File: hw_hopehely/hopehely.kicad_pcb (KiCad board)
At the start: 2 copper layers, 48.3 x 55.8 mm, 39 parts, among them J1 Conn_2Rows-05Pins, Q1 AO3401A, Q2 AO3401A, Q3 AO3401A, SW1 SW_DPST_x2, T1 Tab, U1 PY32F002AF15P6TU

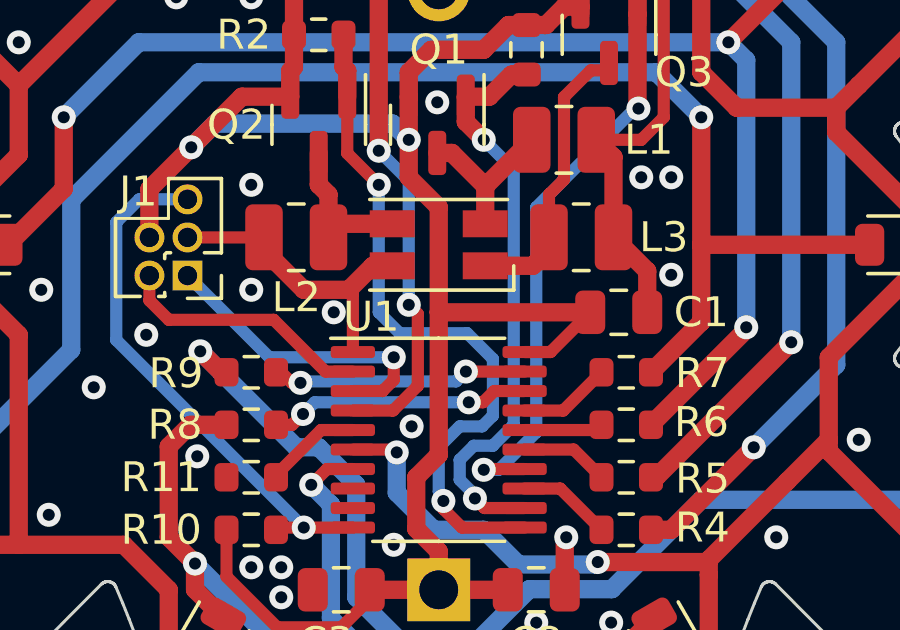
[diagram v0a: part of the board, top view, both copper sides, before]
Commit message: Footprint fix for JLCPCB assembly.
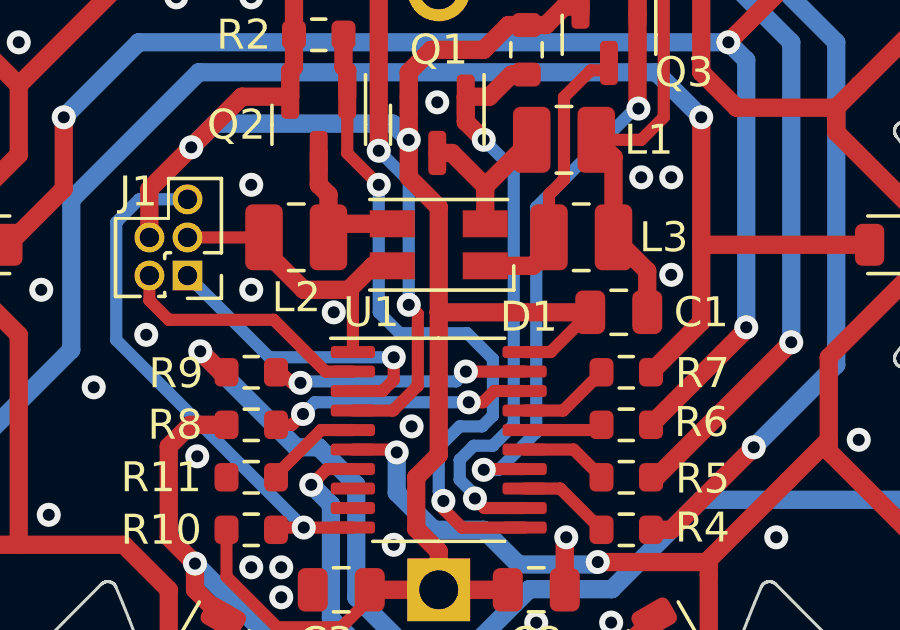
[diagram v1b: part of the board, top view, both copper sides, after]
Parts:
- D1: footprint LED_SMD:LED_RGB_Wuerth-PLCC4_3.2x2.8mm_150141M173100 -> karifa:LED_RGB_Wuerth-PLCC4_3.2x2.8mm_150141M173100
- U1: footprint Package_SO:TSSOP-20_4.4x6.5mm_P0.65mm -> karifa:TSSOP-20_4.4x6.5mm_P0.65mm
- turned D1 to 0 degrees
- turned U1 to 180 degrees

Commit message: Hópehely panelized.
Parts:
- added T1: Tab, kikit:Tab, F.Cu at (182.2, 46.1)
- added T1: Tab, kikit:Tab, F.Cu at (162.2, 63.6)
- added T1: Tab, kikit:Tab, F.Cu at (190.2, 96.6)
- added T1: Tab, kikit:Tab, F.Cu at (209.9, 63.6)
- added T1: Tab, kikit:Tab, F.Cu at (161.7, 79.6)
- moved T1 0.65 mm to (210.0, 79.6)
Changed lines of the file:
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@@
     )
+  )
+  (footprint "kikit:Tab" (layer "F.Cu")
+    (at 182.188176 46.13035 -90)
+    (descr "A symbol representing annotation for tab placement")
+    (property "Sheetfile" "hopehely.kicad_sch")
+    (property "Sheetname" "")
+    (property "exclude_from_bom" "")
+    (property "ki_description" "KiKit tab annotations")
+    (property "ki_keywords" "KiKit")
+    (attr exclude_from_pos_files exclude_from_bom)
+    (fp_text reference "T1" (at 0 -2 90) (layer "F.SilkS") hide
+        (effects (font (size 1 1) (thickness 0.15)))
+    )
+    (fp_text value "Tab" (at -2.75 -1 90) (layer "Dwgs.User")
+        (effects (font (size 1.2 1.2) (thickness 0.2)))
+    )
+    (fp_text user "KIKIT: width: 2mm" (at -5.5 0) (layer "Dwgs.User")
+        (effects (font (size 1 1) (thickness 0.15)))
+    )
+    (fp_line (start 0.25 0) (end -2.75 0)
+      (stroke (width 0.3) (type solid)) (layer "Dwgs.User"))
+    (fp_line (start 0.25 0) (end -0.75 -1)
+      (stroke (width 0.3) (type solid)) (layer "Dwgs.User"))
+    (fp_line (start 0.25 0) (end -0.75 1)
+      (stroke (width 0.3) (type solid)) (layer "Dwgs.User"))
+    (fp_line (start 0.25 1) (end 0.25 -1)
+      (stroke (width 0.3) (type solid)) (layer "Dwgs.User"))
   )
   (footprint "LED_SMD:LED_0805_2012Metric" (layer "F.Cu")
@@
   )
   (footprint "kikit:Tab" (layer "F.Cu")
-    (at 209.988176 78.98035 180)
+    (at 162.188176 63.63035)
     (descr "A symbol representing annotation for tab placement")
     (property "Sheetfile" "hopehely.kicad_sch")
@@
         (effects (font (size 1.2 1.2) (thickness 0.2)))
     )
-    (fp_text user "KIKIT: width: 1.9mm" (at -5.5 0 90) (layer "Dwgs.User")
+    (fp_text user "KIKIT: width: 2mm" (at -5.5 0 90) (layer "Dwgs.User")
+        (effects (font (size 1 1) (thickness 0.15)))
+    )
+    (fp_line (start 0.25 0) (end -2.75 0)
+      (stroke (width 0.3) (type solid)) (layer "Dwgs.User"))
+    (fp_line (start 0.25 0) (end -0.75 -1)
+      (stroke (width 0.3) (type solid)) (layer "Dwgs.User"))
+    (fp_line (start 0.25 0) (end -0.75 1)
+      (stroke (width 0.3) (type solid)) (layer "Dwgs.User"))
+    (fp_line (start 0.25 1) (end 0.25 -1)
+      (stroke (width 0.3) (type solid)) (layer "Dwgs.User"))
+  )
+  (footprint "kikit:Tab" (layer "F.Cu")
+    (at 209.988176 79.63035 180)
+    (descr "A symbol representing annotation for tab placement")
+    (property "Sheetfile" "hopehely.kicad_sch")
+    (property "Sheetname" "")
+    (property "exclude_from_bom" "")
+    (property "ki_description" "KiKit tab annotations")
+    (property "ki_keywords" "KiKit")
+    (attr exclude_from_pos_files exclude_from_bom)
+    (fp_text reference "T1" (at 0 -2) (layer "F.SilkS") hide
+        (effects (font (size 1 1) (thickness 0.15)))
+    )
+    (fp_text value "Tab" (at -2.75 -1) (layer "Dwgs.User")
+        (effects (font (size 1.2 1.2) (thickness 0.2)))
+    )
+    (fp_text user "KIKIT: width: 2mm" (at -5.5 0 90) (layer "Dwgs.User")
         (effects (font (size 1 1) (thickness 0.15)))
     )
@@
     )
   )
+  (footprint "kikit:Tab" (layer "F.Cu")
+    (at 190.188176 96.63035 90)
+    (descr "A symbol representing annotation for tab placement")
+    (property "Sheetfile" "hopehely.kicad_sch")
+    (property "Sheetname" "")
+    (property "exclude_from_bom" "")
+    (property "ki_description" "KiKit tab annotations")
+    (property "ki_keywords" "KiKit")
+    (attr exclude_from_pos_files exclude_from_bom)
+    (fp_text reference "T1" (at 0 -2 90) (layer "F.SilkS") hide
+        (effects (font (size 1 1) (thickness 0.15)))
+    )
+    (fp_text value "Tab" (at -2.75 -1 90) (layer "Dwgs.User")
+        (effects (font (size 1.2 1.2) (thickness 0.2)))
+    )
+    (fp_text user "KIKIT: width: 2mm" (at -5.5 0) (layer "Dwgs.User")
+        (effects (font (size 1 1) (thickness 0.15)))
+    )
+    (fp_line (start 0.25 0) (end -2.75 0)
+      (stroke (width 0.3) (type solid)) (layer "Dwgs.User"))
+    (fp_line (start 0.25 0) (end -0.75 -1)
+      (stroke (width 0.3) (type solid)) (layer "Dwgs.User"))
+    (fp_line (start 0.25 0) (end -0.75 1)
+      (stroke (width 0.3) (type solid)) (layer "Dwgs.User"))
+    (fp_line (start 0.25 1) (end 0.25 -1)
+      (stroke (width 0.3) (type solid)) (layer "Dwgs.User"))
+  )
   (footprint "Resistor_SMD:R_0603_1608Metric" (layer "F.Cu")
     (at 179.938176 77.63035)
@@
       (rotate (xyz 0 0 0))
     )
+  )
+  (footprint "kikit:Tab" (layer "F.Cu")
+    (at 209.938176 63.63035 180)
+    (descr "A symbol representing annotation for tab placement")
+    (property "Sheetfile" "hopehely.kicad_sch")
+    (property "Sheetname" "")
+    (property "exclude_from_bom" "")
+    (property "ki_description" "KiKit tab annotations")
+    (property "ki_keywords" "KiKit")
+    (attr exclude_from_pos_files exclude_from_bom)
+    (fp_text reference "T1" (at 0 -2) (layer "F.SilkS") hide
+        (effects (font (size 1 1) (thickness 0.15)))
+    )
+    (fp_text value "Tab" (at -2.75 -1) (layer "Dwgs.User")
+        (effects (font (size 1.2 1.2) (thickness 0.2)))
+    )
+    (fp_text user "KIKIT: width: 2mm" (at -5.5 0 90) (layer "Dwgs.User")
+        (effects (font (size 1 1) (thickness 0.15)))
+    )
+    (fp_line (start 0.25 0) (end -2.75 0)
+      (stroke (width 0.3) (type solid)) (layer "Dwgs.User"))
+    (fp_line (start 0.25 0) (end -0.75 -1)
+      (stroke (width 0.3) (type solid)) (layer "Dwgs.User"))
+    (fp_line (start 0.25 0) (end -0.75 1)
+      (stroke (width 0.3) (type solid)) (layer "Dwgs.User"))
+    (fp_line (start 0.25 1) (end 0.25 -1)
+      (stroke (width 0.3) (type solid)) (layer "Dwgs.User"))
   )
   (footprint "LED_SMD:LED_0805_2012Metric" (layer "F.Cu")
@@
     )
   )
+  (footprint "kikit:Tab" (layer "F.Cu")
+    (at 161.688176 79.63035)
+    (descr "A symbol representing annotation for tab placement")
+    (property "Sheetfile" "hopehely.kicad_sch")
+    (property "Sheetname" "")
+    (property "exclude_from_bom" "")
+    (property "ki_description" "KiKit tab annotations")
+    (property "ki_keywords" "KiKit")
+    (attr exclude_from_pos_files exclude_from_bom)
+    (fp_text reference "T1" (at 0 -2) (layer "F.SilkS") hide
+        (effects (font (size 1 1) (thickness 0.15)))
+    )
+    (fp_text value "Tab" (at -2.75 -1) (layer "Dwgs.User")
+        (effects (font (size 1.2 1.2) (thickness 0.2)))
+    )
+    (fp_text user "KIKIT: width: 2mm" (at -5.5 0 90) (layer "Dwgs.User")
+        (effects (font (size 1 1) (thickness 0.15)))
+    )
+    (fp_line (start 0.25 0) (end -2.75 0)
+      (stroke (width 0.3) (type solid)) (layer "Dwgs.User"))
+    (fp_line (start 0.25 0) (end -0.75 -1)
+      (stroke (width 0.3) (type solid)) (layer "Dwgs.User"))
+    (fp_line (start 0.25 0) (end -0.75 1)
+      (stroke (width 0.3) (type solid)) (layer "Dwgs.User"))
+    (fp_line (start 0.25 1) (end 0.25 -1)
+      (stroke (width 0.3) (type solid)) (layer "Dwgs.User"))
+  )
   (footprint "karifa:CR2032_Holder" locked (layer "B.Cu")
